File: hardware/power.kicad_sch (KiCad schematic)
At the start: 23 parts, among them T2 PA2748NL, U2 LM2596S-3.3, U2 LM2596SX-ADJ, U5 LM2596S-5

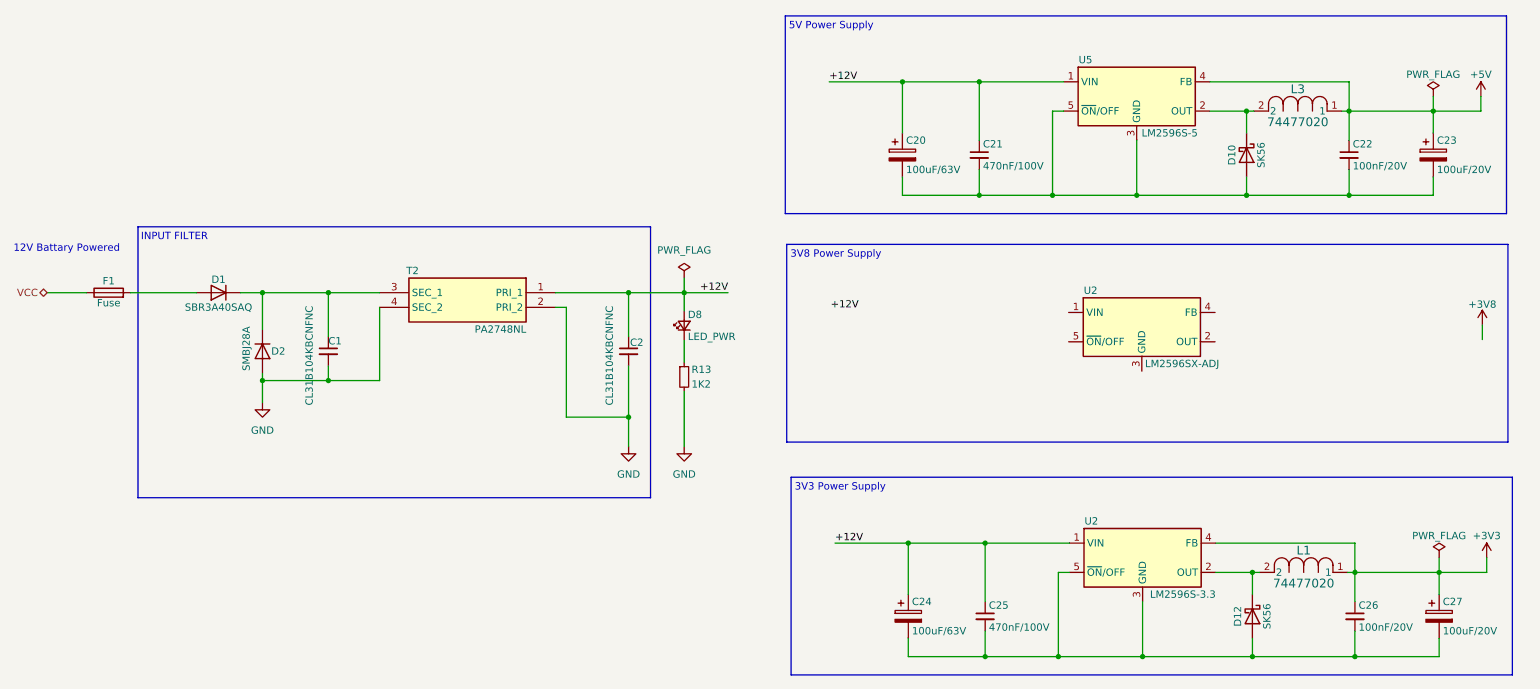
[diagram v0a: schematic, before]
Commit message: 3V8 modules completed
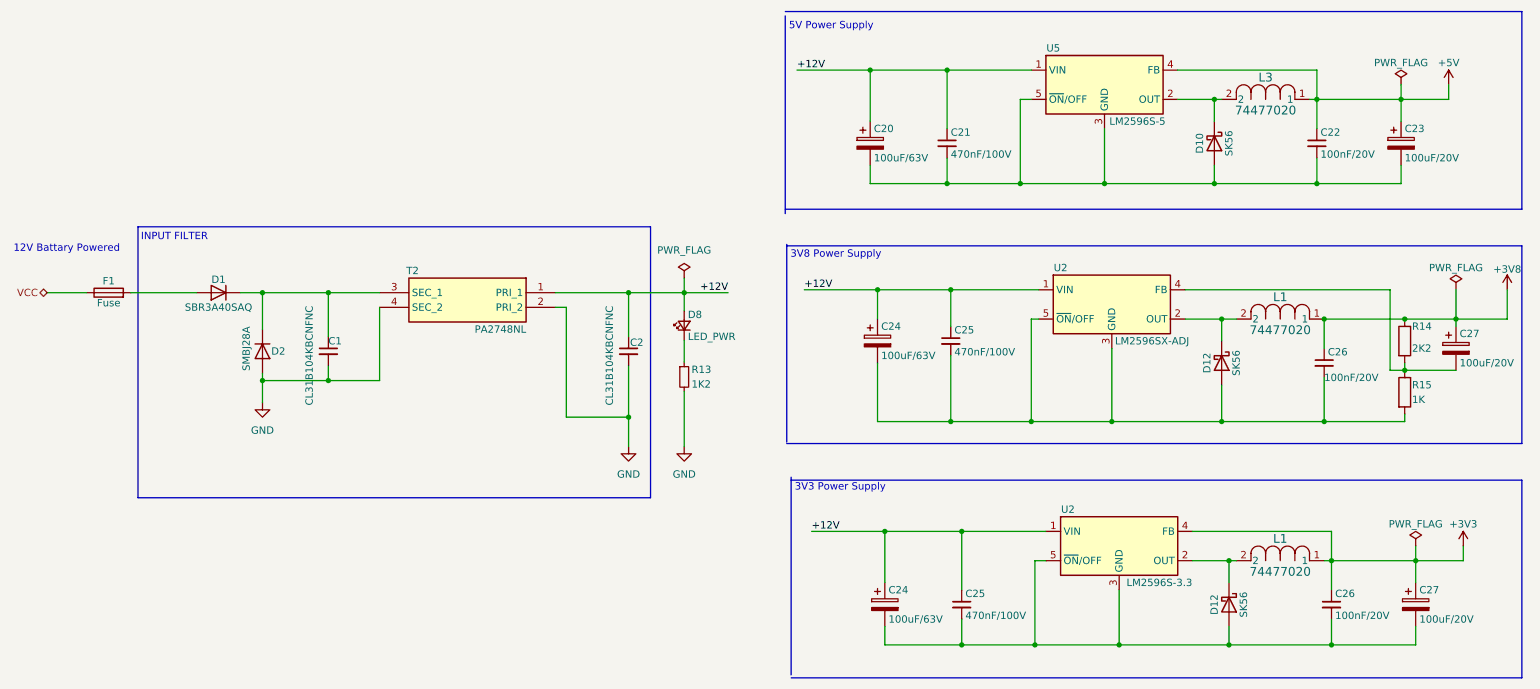
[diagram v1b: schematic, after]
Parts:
- added C24: 100uF/63V, Capacitor_SMD:CP_Elec_10x10.5, symbol Device:C_Polarized
- added C25: 470nF/100V, Capacitor_SMD:C_1206_3216Metric, symbol Device:C_Small
- added C26: 100nF/20V, Capacitor_SMD:C_0805_2012Metric, symbol Device:C_Small
- added C27: 100uF/20V, Capacitor_SMD:CP_Elec_6.3x7.7, symbol Device:C_Polarized
- added D12: SK56, Diode_SMD:D_SMC, symbol Device:D_Schottky
- added L1: 74477020, Damlama:IND_1280-WE-PD_WRE, symbol Damlama:74477020
- added R14: 2K2, symbol Device:R
- added R15: 1K, symbol Device:R
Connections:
- net +12V: now also U2.1 (VIN), C24.1, C25.1
- net +3V8: now also C26.1, C27.1, L1.1, R14.1
- net at U2.2 (OUT): now also D12.1 (K), L1.2
- net at U2.3 (GND): now also U2.5 (~{ON}/OFF), C24.2, C25.2, C26.2, D12.2 (A), R15.2
- net at U2.4 (FB): now also C27.2, R14.2, R15.1
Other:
- moved on the sheet: C20, C21, C22, C23, C24, C25, C26, C27, D10, D12, L1, L3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
